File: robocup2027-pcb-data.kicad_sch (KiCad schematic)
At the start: 46 parts, among them M5 Motor_Servo, M6 Motor_Servo, Q1 BPW40, Q2 BPW40, U1 ESP32-DEVKITC-32E

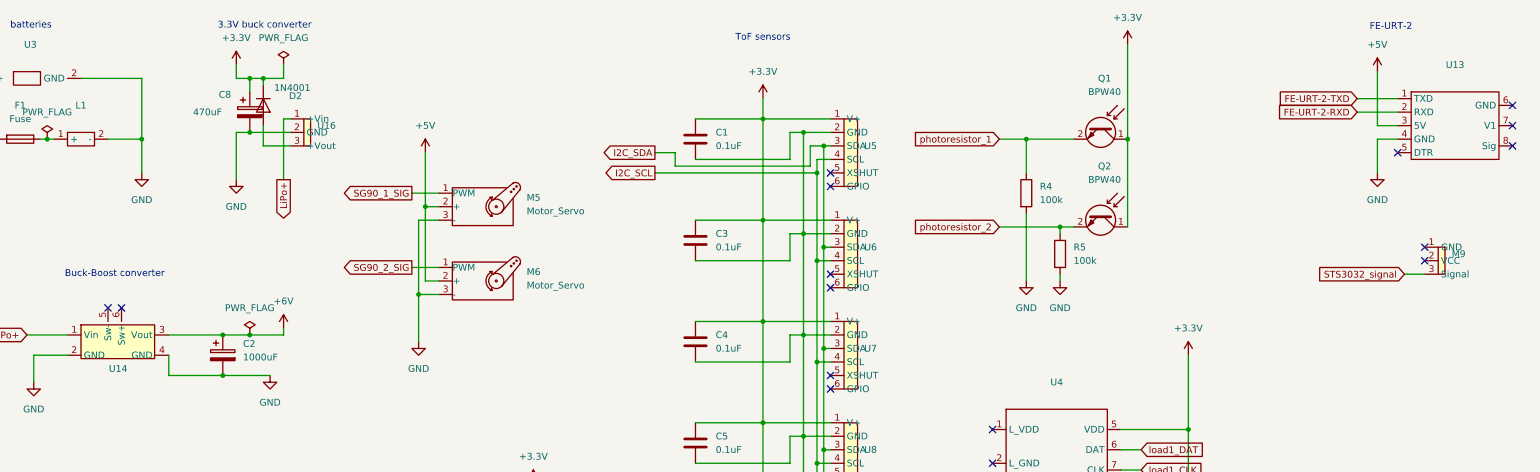
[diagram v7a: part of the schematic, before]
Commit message: fixing extra pins to match with footprints
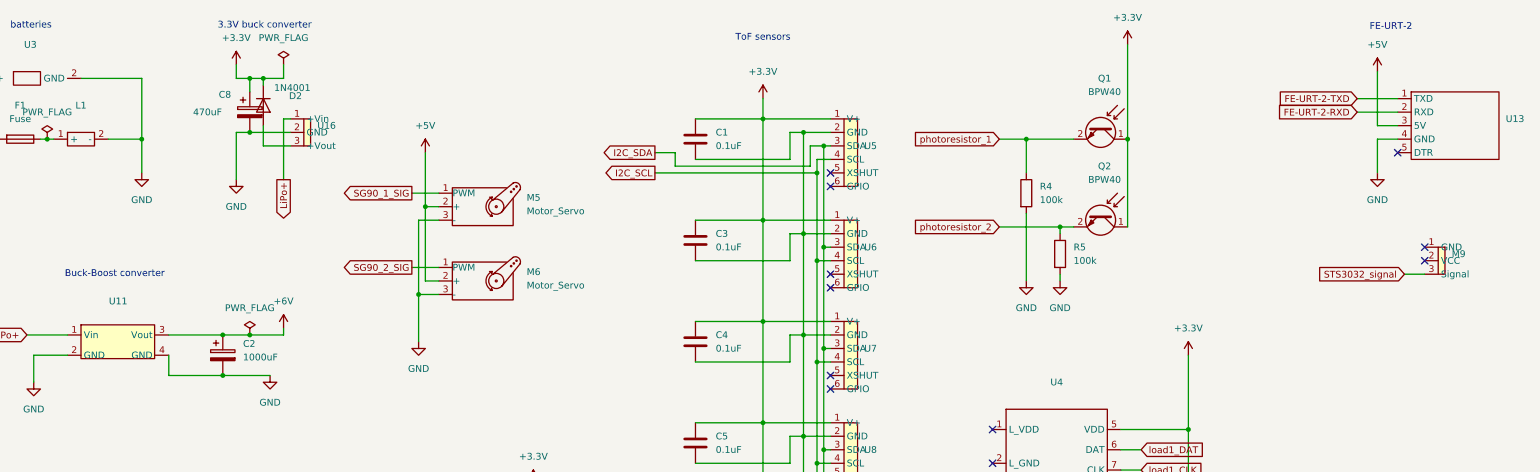
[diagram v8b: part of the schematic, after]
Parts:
- removed U14: ~, robo:DCDC-LTC3111, symbol robo:DCDC-LTC3111
- added U11: ~, robo:DCDC-LTC3111, symbol robo:DCDC-LTC3111
- U13: footprint robo:fe-urt-2 -> (none)
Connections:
- net +6V: now also U11.3 (Vout)
- net GND: now also U11.2 (GND), U11.4 (GND)
- net LiPo+: now also U11.1 (Vin)
- no-connect marks 54 -> 49
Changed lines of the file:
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@@
 	)
 	(no_connect
-		(at 64.77 69.85)
-	)
-	(no_connect
 		(at 255.27 104.14)
 	)
@@
 	)
 	(no_connect
-		(at 328.93 31.75)
-	)
-	(no_connect
 		(at 134.62 140.97)
 	)
@@
 	)
 	(no_connect
-		(at 67.31 69.85)
-	)
-	(no_connect
 		(at 231.14 92.71)
 	)
@@
 	)
 	(no_connect
-		(at 328.93 35.56)
-	)
-	(no_connect
 		(at 134.62 166.37)
 	)
@@
 	)
 	(no_connect
-		(at 328.93 39.37)
-	)
-	(no_connect
 		(at 312.42 60.96)
 	)
@@
 	)
 	(symbol
+		(lib_id "robo:fe-urt-2")
+		(at 314.96 35.56 0)
+		(unit 1)
+		(exclude_from_sim no)
+		(in_bom yes)
+		(on_board yes)
+		(dnp no)
+		(fields_autoplaced yes)
+		(property "Reference" "U13"
+			(at 327.66 34.2899 0)
+			(effects
+				(font
+					(size 1.27 1.27)
+				)
+				(justify left)
+			)
+		)
+		(property "Value" "~"
+			(at 327.66 36.8299 0)
+			(effects
+				(font
+					(size 1.27 1.27)
+				)
+				(justify left)
+			)
+		)
+		(property "Footprint" ""
+			(at 314.96 35.56 0)
+			(effects
+				(font
+					(size 1.27 1.27)
+				)
+				(hide yes)
+			)
+		)
+		(property "Datasheet" ""
+			(at 314.96 35.56 0)
+			(effects
+				(font
+					(size 1.27 1.27)
+				)
+				(hide yes)
+			)
+		)
+		(property "Description" ""
+			(at 314.96 35.56 0)
+			(effects
+				(font
+					(size 1.27 1.27)
+				)
+				(hide yes)
+			)
+		)
+		(pin "1"
+		)
+		(pin "5"
+		)
+		(pin "4"
+		)
+		(pin "2"
+		)
+		(pin "3"
+		)
+		(instances
+			(project "robocup2027-pcb-data"
+				(path "/fda8bdee-4e79-4e78-9174-7c0702f316a4"
+					(reference "U13")
+					(unit 1)
+				)
+			)
+		)
+	)
+	(symbol
 		(lib_id "power:PWR_FLAG")
 		(at 138.43 123.19 0)
@@
 	)
 	(symbol
-		(lib_id "robo:DCDC-LTC3111")
-		(at 66.04 76.2 0)
-		(unit 1)
-		(exclude_from_sim no)
-		(in_bom yes)
-		(on_board yes)
-		(dnp no)
-		(fields_autoplaced yes)
-		(property "Reference" "U14"
-			(at 66.675 81.28 0)
-			(effects
-				(font
-					(size 1.27 1.27)
-				)
-			)
-		)
-		(property "Value" "~"
-			(at 66.675 83.82 0)
-			(effects
-				(font
-					(size 1.27 1.27)
-				)
-			)
-		)
-		(property "Footprint" "robo:DCDC-LTC3111"
-			(at 66.04 76.2 0)
-			(effects
-				(font
-					(size 1.27 1.27)
-				)
-				(hide yes)
-			)
-		)
-		(property "Datasheet" ""
-			(at 66.04 76.2 0)
-			(effects
-				(font
-					(size 1.27 1.27)
-				)
-				(hide yes)
-			)
-		)
-		(property "Description" ""
-			(at 66.04 76.2 0)
-			(effects
-				(font
-					(size 1.27 1.27)
-				)
-				(hide yes)
-			)
-		)
-		(pin "5"
-		)
-		(pin "4"
-		)
-		(pin "2"
-		)
-		(pin "1"
-		)
-		(pin "3"
-		)
-		(pin "6"
-		)
-		(instances
-			(project "robocup2027-pcb-data"
-				(path "/fda8bdee-4e79-4e78-9174-7c0702f316a4"
-					(reference "U14")
-					(unit 1)
-				)
-			)
-		)
-	)
-	(symbol
 		(lib_id "power:GND")
 		(at 123.19 76.2 0)
@@
 	)
 	(symbol
-		(lib_id "robo:fe-urt-2")
-		(at 314.96 35.56 0)
-		(unit 1)
-		(exclude_from_sim no)
-		(in_bom yes)
-		(on_board yes)
-		(dnp no)
-		(fields_autoplaced yes)
-		(property "Reference" "U13"
-			(at 318.135 24.13 0)
-			(effects
-				(font
-					(size 1.27 1.27)
-				)
-			)
-		)
-		(property "Value" "~"
-			(at 318.135 26.67 0)
-			(effects
-				(font
-					(size 1.27 1.27)
-				)
-			)
-		)
-		(property "Footprint" "robo:fe-urt-2"
-			(at 314.96 35.56 0)
-			(effects
-				(font
-					(size 1.27 1.27)
-				)
-				(hide yes)
-			)
-		)
-		(property "Datasheet" ""
-			(at 314.96 35.56 0)
-			(effects
-				(font
-					(size 1.27 1.27)
-				)
-				(hide yes)
-			)
-		)
-		(property "Description" ""
-			(at 314.96 35.56 0)
-			(effects
-				(font
-					(size 1.27 1.27)
-				)
-				(hide yes)
-			)
-		)
-		(pin "8"
-		)
-		(pin "5"
-		)
-		(pin "6"
-		)
-		(pin "2"
-		)
-		(pin "1"
-		)
-		(pin "7"
-		)
-		(pin "4"
-		)
-		(pin "3"
-		)
-		(instances
-			(project "robocup2027-pcb-data"
-				(path "/fda8bdee-4e79-4e78-9174-7c0702f316a4"
-					(reference "U13")
-					(unit 1)
-				)
-			)
-		)
-	)
-	(symbol
 		(lib_id "robo:tactile switch")
 		(at 86.36 133.35 270)
@@
 					(unit 1)
 				)
+			)
+		)
+	)
+	(symbol
+		(lib_id "robo:DCDC-LTC3111")
+		(at 66.04 76.2 0)
+		(unit 1)
+		(exclude_from_sim no)
+		(in_bom yes)
+		(on_board yes)
+		(dnp no)
+		(fields_autoplaced yes)
+		(property "Reference" "U11"
+			(at 66.675 68.58 0)
+			(effects
+				(font
+					(size 1.27 1.27)
+				)
+			)
+		)
+		(property "Value" "~"
+			(at 66.675 71.12 0)
+			(effects
+				(font
+					(size 1.27 1.27)
+				)
+			)
+		)
+		(property "Footprint" "robo:DCDC-LTC3111"
+			(at 66.04 76.2 0)
+			(effects
+				(font
+					(size 1.27 1.27)
+				)
+				(hide yes)
+			)
+		)
+		(property "Datasheet" ""
+			(at 66.04 76.2 0)
+			(effects
+				(font
+					(size 1.27 1.27)
+				)
+				(hide yes)
+			)
+		)
+		(property "Description" ""
+			(at 66.04 76.2 0)
+			(effects
+				(font
+					(size 1.27 1.27)
+				)
+				(hide yes)
+			)
+		)
+		(pin "3"
+		)
+		(pin "4"
+		)
+		(pin "2"
+		)
+		(pin "1"
+		)
+		(instances
+			(project "robocup2027-pcb-data"
+				(path "/fda8bdee-4e79-4e78-9174-7c0702f316a4"
+					(reference "U11")
+					(unit 1)
+				)
